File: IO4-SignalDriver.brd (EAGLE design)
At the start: 106 x 100 mm, 25 parts, among them CON2 CONNECTOR-GROVE-4P-2.0-347013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, CON3 CONNECTOR-GROVE-4P-2.0-347013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, IC1 74LS139D, P1 500R, P2 500R, P3 500R, P4 500R, P5 500R, P6 500R

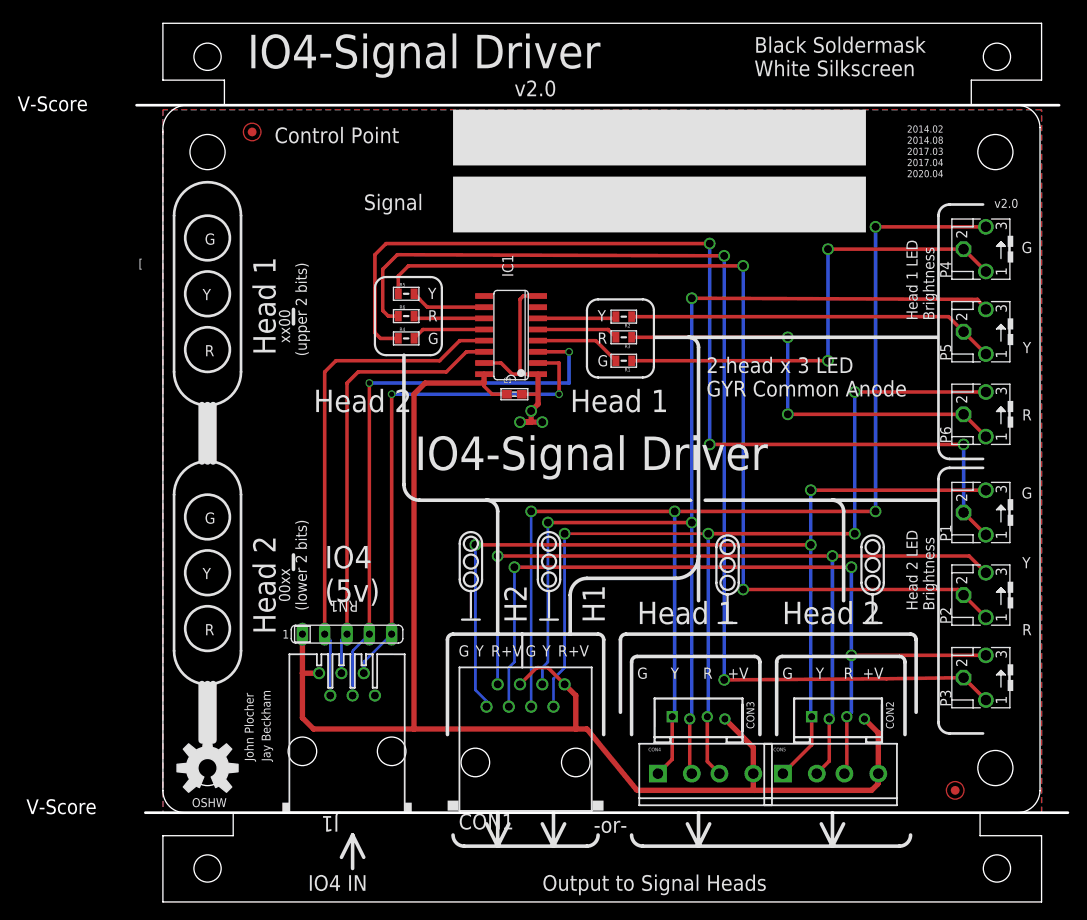
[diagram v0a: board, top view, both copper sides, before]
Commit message: FID placement & SPCoast update
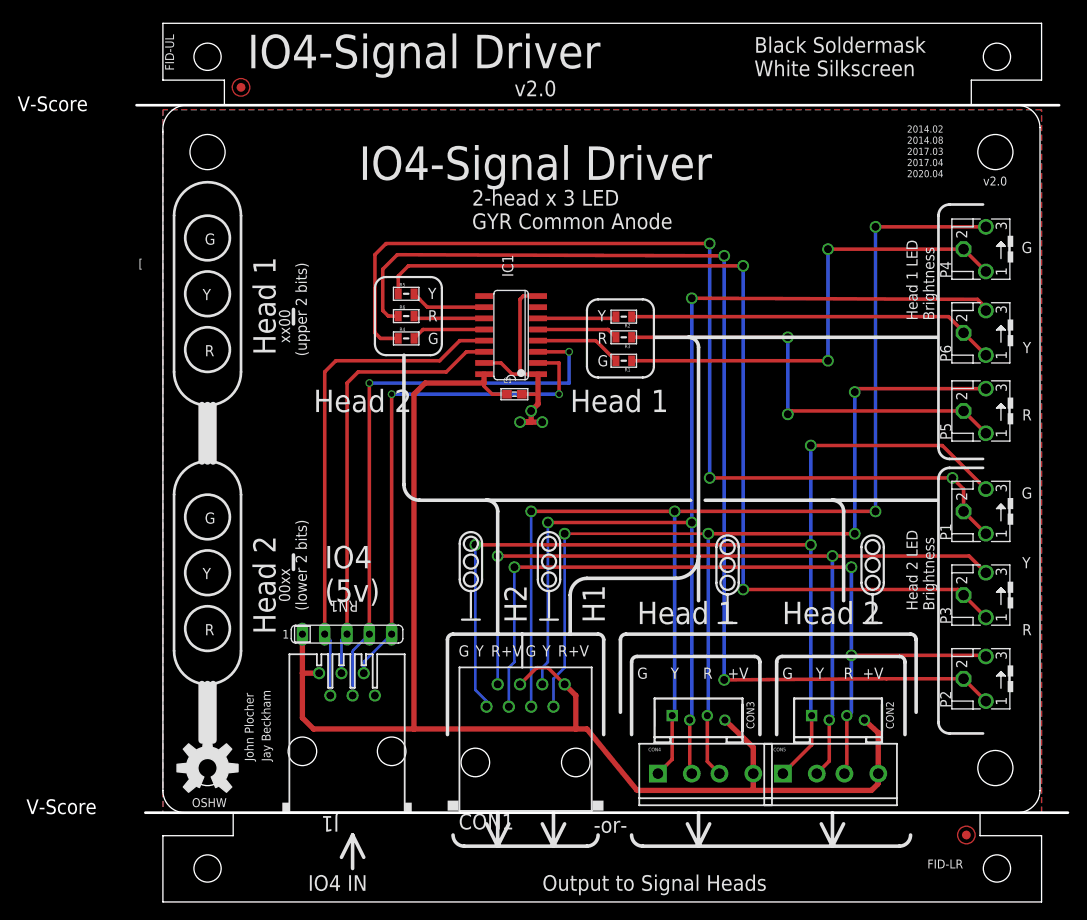
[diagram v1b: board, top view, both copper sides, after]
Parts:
- removed FID1, FID2: FIDUCIAL, SPCoast:FIDUCIAL_1MM
- added FID-LR, FID-UL: FIDUCIAL, SPCoast:FIDUCIAL_1MM
- CON2, CON3: value CONNECTOR-GROVE-4P-2.0-3470130P1 -> (none)
- moved P2 9.52 mm to (93.3, 25.4)
- moved P3 9.40 mm to (93.3, 34.9)
- moved P6 9.27 mm to (93.3, 64.8)
- moved P5 9.02 mm to (93.3, 55.9)
- moved P1 0.13 mm to (93.3, 44.5)
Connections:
- net G1-LED: now also P1.3; no longer P1.CW
- net G1V: now also P1.1, P1.2; no longer P1.CCW, P1.W
- net G2-LED: now also P4.3; no longer P4.CW
- net G2V: now also P4.1, P4.2; no longer P4.CCW, P4.W
- net R1-LED: now also P2.3; no longer P3.CW
- net R1V: now also P2.1, P2.2; no longer P3.CCW, P3.W
- net R2-LED: now also P5.3; no longer P6.CW
- net R2V: now also P5.1, P5.2; no longer P6.CCW, P6.W
- net Y1-LED: now also P3.3; no longer P2.CW
- net Y1V: now also P3.1, P3.2; no longer P2.CCW, P2.W
- net Y2-LED: now also P6.3; no longer P5.CW
- net Y2V: now also P6.1, P6.2; no longer P5.CCW, P5.W
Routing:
- net G1-LED: track 110.7 -> 117.9 mm
- net G1V: track 113.5 -> 112.7 mm
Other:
- board text added: "Changes: Silk Screen alignment, tweeking spaced fixed resistors further apart min trace width 16mil SMT components 2mmx4 headers SPCoast lbr update (Pots) FIDs"
- board text removed: "Changes: Silk Screen alignment, tweeking spaced fixed resistors further apart min trace width 16mil SMT components 2mmx4 headers"
- board text removed: "Control Point"
- board text removed: "Signal"

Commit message: added values for connectors
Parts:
- CON1: value (none) -> RJ45
- CON2, CON3: value (none) -> 2mm
- CON4, CON5: value (none) -> 3.5mm
- J1: value (none) -> RJ12/6
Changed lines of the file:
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@@
 <grid distance="50" unitdist="mil" unit="mil" style="dots" multiple="2" display="yes" altdistance="25" altunitdist="mil" altunit="mil"/>
 <layers>
-<layer number="1" name="Top" color="4" fill="1" visible="no" active="yes"/>
-<layer number="16" name="Bottom" color="2" fill="1" visible="no" active="yes"/>
+<layer number="1" name="Top" color="4" fill="1" visible="yes" active="yes"/>
+<layer number="16" name="Bottom" color="2" fill="1" visible="yes" active="yes"/>
 <layer number="17" name="Pads" color="23" fill="1" visible="yes" active="yes"/>
 <layer number="18" name="Vias" color="23" fill="1" visible="yes" active="yes"/>
-<layer number="19" name="Unrouted" color="63" fill="1" visible="no" active="yes"/>
+<layer number="19" name="Unrouted" color="63" fill="1" visible="yes" active="yes"/>
 <layer number="20" name="Dimension" color="15" fill="1" visible="yes" active="yes"/>
 <layer number="21" name="tPlace" color="22" fill="1" visible="yes" active="yes"/>
 <layer number="22" name="bPlace" color="35" fill="1" visible="no" active="yes"/>
-<layer number="23" name="tOrigins" color="29" fill="1" visible="no" active="yes"/>
+<layer number="23" name="tOrigins" color="29" fill="1" visible="yes" active="yes"/>
 <layer number="24" name="bOrigins" color="15" fill="1" visible="no" active="yes"/>
-<layer number="25" name="tNames" color="19" fill="1" visible="no" active="yes"/>
+<layer number="25" name="tNames" color="19" fill="1" visible="yes" active="yes"/>
 <layer number="26" name="bNames" color="34" fill="1" visible="no" active="yes"/>
 <layer number="27" name="tValues" color="56" fill="1" visible="yes" active="yes"/>
@@
 <layer number="42" name="bRestrict" color="3" fill="10" visible="no" active="yes"/>
 <layer number="43" name="vRestrict" color="2" fill="10" visible="no" active="yes"/>
-<layer number="44" name="Drills" color="16" fill="1" visible="no" active="yes"/>
-<layer number="45" name="Holes" color="35" fill="1" visible="no" active="yes"/>
-<layer number="46" name="Milling" color="25" fill="1" visible="no" active="yes"/>
-<layer number="47" name="Measures" color="21" fill="1" visible="no" active="yes"/>
+<layer number="44" name="Drills" color="16" fill="1" visible="yes" active="yes"/>
+<layer number="45" name="Holes" color="35" fill="1" visible="yes" active="yes"/>
+<layer number="46" name="Milling" color="25" fill="1" visible="yes" active="yes"/>
+<layer number="47" name="Measures" color="21" fill="1" visible="yes" active="yes"/>
 <layer number="48" name="Document" color="15" fill="1" visible="yes" active="yes"/>
-<layer number="49" name="Reference" color="48" fill="1" visible="no" active="yes"/>
+<layer number="49" name="Reference" color="48" fill="1" visible="yes" active="yes"/>
 <layer number="50" name="dxf" color="7" fill="1" visible="no" active="yes"/>
 <layer number="51" name="tDocu" color="24" fill="1" visible="yes" active="yes"/>
@@
 <layer number="98" name="Guide" color="6" fill="1" visible="no" active="no"/>
 <layer number="99" name="Anatomie" color="7" fill="1" visible="no" active="no"/>
-<layer number="101" name="Patch_Top" color="20" fill="1" visible="no" active="yes"/>
+<layer number="101" name="Patch_Top" color="20" fill="1" visible="yes" active="yes"/>
 <layer number="2" name="Route2" color="1" fill="3" visible="no" active="no"/>
 <layer number="3" name="Route3" color="4" fill="3" visible="no" active="no"/>
@@
 <attribute name="VALUE" x="26.67" y="62.738" size="0.4064" layer="27"/>
 </element>
-<element name="CON4" library="SparkFun" package="SCREWTERMINAL-3.5MM-4_LOCK" value="" x="56.515" y="14.605"/>
-<element name="CON5" library="SparkFun" package="SCREWTERMINAL-3.5MM-4_LOCK" value="" x="70.739" y="14.605"/>
+<element name="CON4" library="SparkFun" package="SCREWTERMINAL-3.5MM-4_LOCK" value="3.5mm" x="56.515" y="14.605"/>
+<element name="CON5" library="SparkFun" package="SCREWTERMINAL-3.5MM-4_LOCK" value="3.5mm" x="70.739" y="14.605"/>
 <element name="RN1" library="resistor-sil" package="SIL5" value="4k7" x="20.955" y="30.48" smashed="yes">
 <attribute name="MF" value="" x="20.955" y="30.48" size="1.778" layer="27" display="off"/>
@@
 <attribute name="VALUE" x="29.21" y="29.845" size="1.27" layer="27" ratio="10" rot="SR90"/>
 </element>
-<element name="J1" library="SPCoast" package="RJ25-PANEL" value="" x="20.955" y="17.145" smashed="yes">
+<element name="J1" library="SPCoast" package="RJ25-PANEL" value="RJ12/6" x="20.955" y="17.145" smashed="yes">
 <attribute name="NAME" x="20.066" y="9.779" size="1.778" layer="25" rot="SR180"/>
 <attribute name="VALUE" x="29.845" y="12.319" size="1.778" layer="27" rot="R90"/>
@@
 <attribute name="AMP" value="520250-3" x="20.955" y="17.145" size="1.778" layer="27" display="off"/>
 </element>
-<element name="CON1" library="SPCoast" package="RJ45-NO-SHIELD" value="" x="41.275" y="15.875">
+<element name="CON1" library="SPCoast" package="RJ45-NO-SHIELD" value="RJ45" x="41.275" y="15.875">
 <attribute name="AMP" value="520151-4" x="41.275" y="15.875" size="1.778" layer="27" display="off"/>
 <attribute name="OPL" value="none" x="41.275" y="15.875" size="1.778" layer="27" display="off"/>
@@
 <element name="BOARD1" library="SPCoast" package="BOARD-DINRAIL-3.17INX10CM" value="BOARD80X100" x="0" y="0"/>
 <element name="U$2" library="SparkFun" package="OSHW-LOGO-L" value="OSHW-LOGOL" x="5.08" y="15.24"/>
-<element name="CON2" library="SPCoast" package="4P-2.0" value="" x="76.835" y="20.955" smashed="yes">
+<element name="CON2" library="SPCoast" package="4P-2.0" value="2mm" x="76.835" y="20.955" smashed="yes">
 <attribute name="NAME" x="83.185" y="19.685" size="0.889" layer="21" font="vector" ratio="11" rot="R90"/>
 </element>
-<element name="CON3" library="SPCoast" package="4P-2.0" value="" x="60.96" y="20.955" smashed="yes">
+<element name="CON3" library="SPCoast" package="4P-2.0" value="2mm" x="60.96" y="20.955" smashed="yes">
 <attribute name="NAME" x="67.31" y="19.685" size="0.889" layer="21" font="vector" ratio="11" rot="R90"/>
 </element>

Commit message: normalized values
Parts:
- BOARD1: value BOARD80X100 -> BOARD
- U$2: value OSHW-LOGOL -> OSHW
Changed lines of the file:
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@@
 <attribute name="OPL" value="none" x="41.275" y="15.875" size="1.778" layer="27" display="off"/>
 </element>
-<element name="BOARD1" library="SPCoast" package="BOARD-DINRAIL-3.17INX10CM" value="BOARD80X100" x="0" y="0"/>
-<element name="U$2" library="SparkFun" package="OSHW-LOGO-L" value="OSHW-LOGOL" x="5.08" y="15.24"/>
+<element name="BOARD1" library="SPCoast" package="BOARD-DINRAIL-3.17INX10CM" value="BOARD" x="0" y="0"/>
+<element name="U$2" library="SparkFun" package="OSHW-LOGO-L" value="OSHW" x="5.08" y="15.24"/>
 <element name="CON2" library="SPCoast" package="4P-2.0" value="2mm" x="76.835" y="20.955" smashed="yes">
 <attribute name="NAME" x="83.185" y="19.685" size="0.889" layer="21" font="vector" ratio="11" rot="R90"/>
